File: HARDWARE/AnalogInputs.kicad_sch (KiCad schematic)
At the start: 12 parts, among them U7 MCP6001-OT, U8 MCP6001-OT

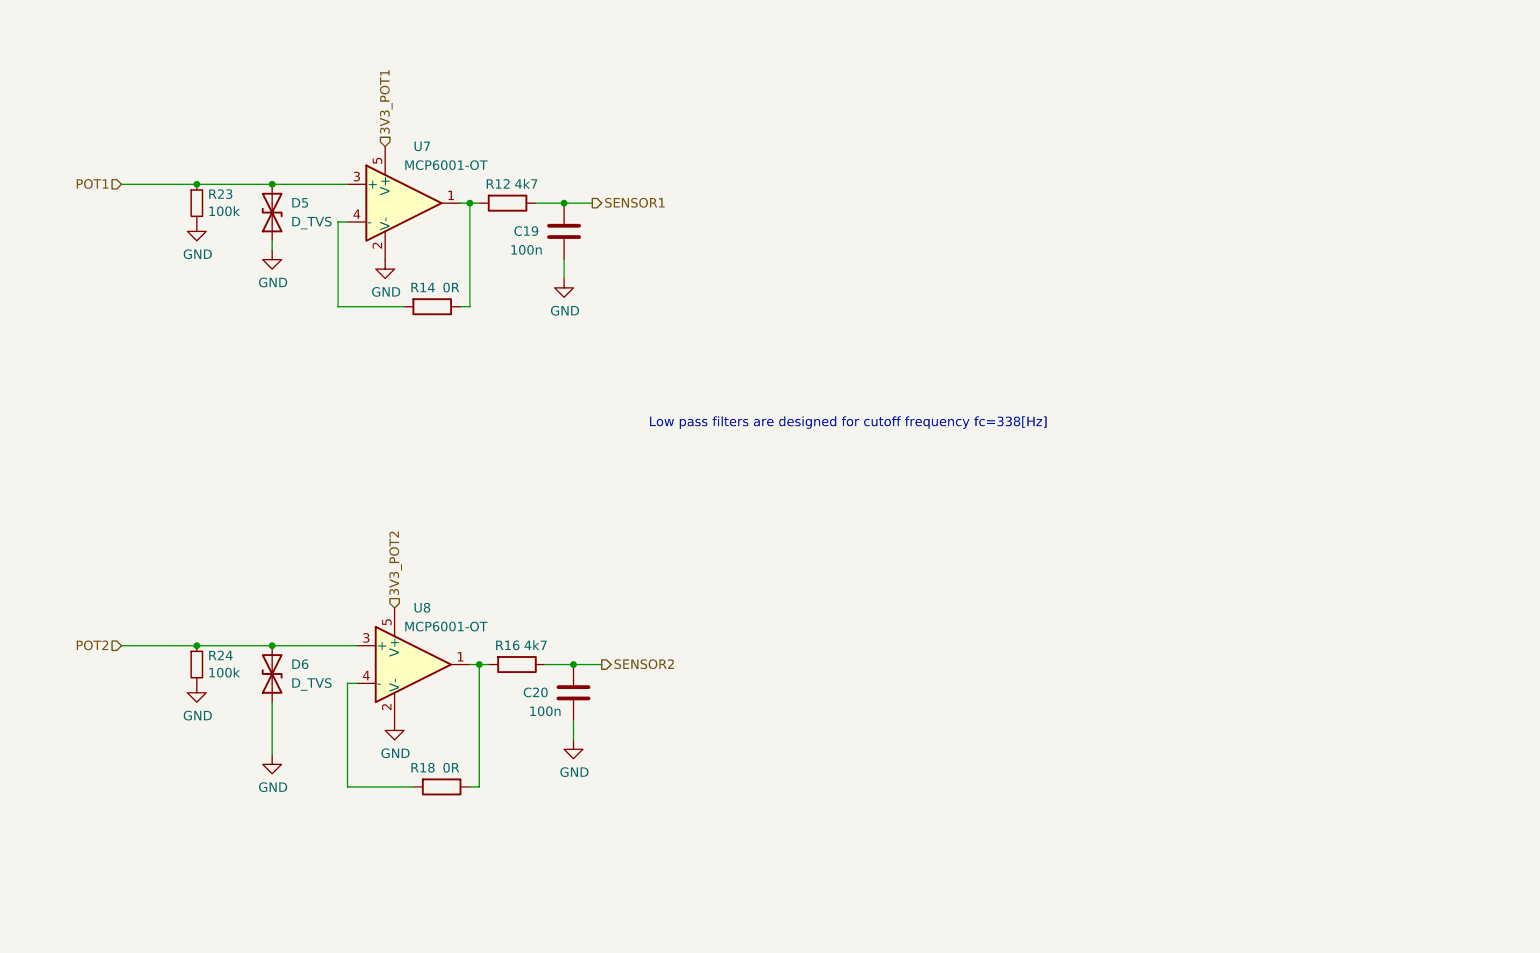
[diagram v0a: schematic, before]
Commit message: Use in-amps for the analog inputs
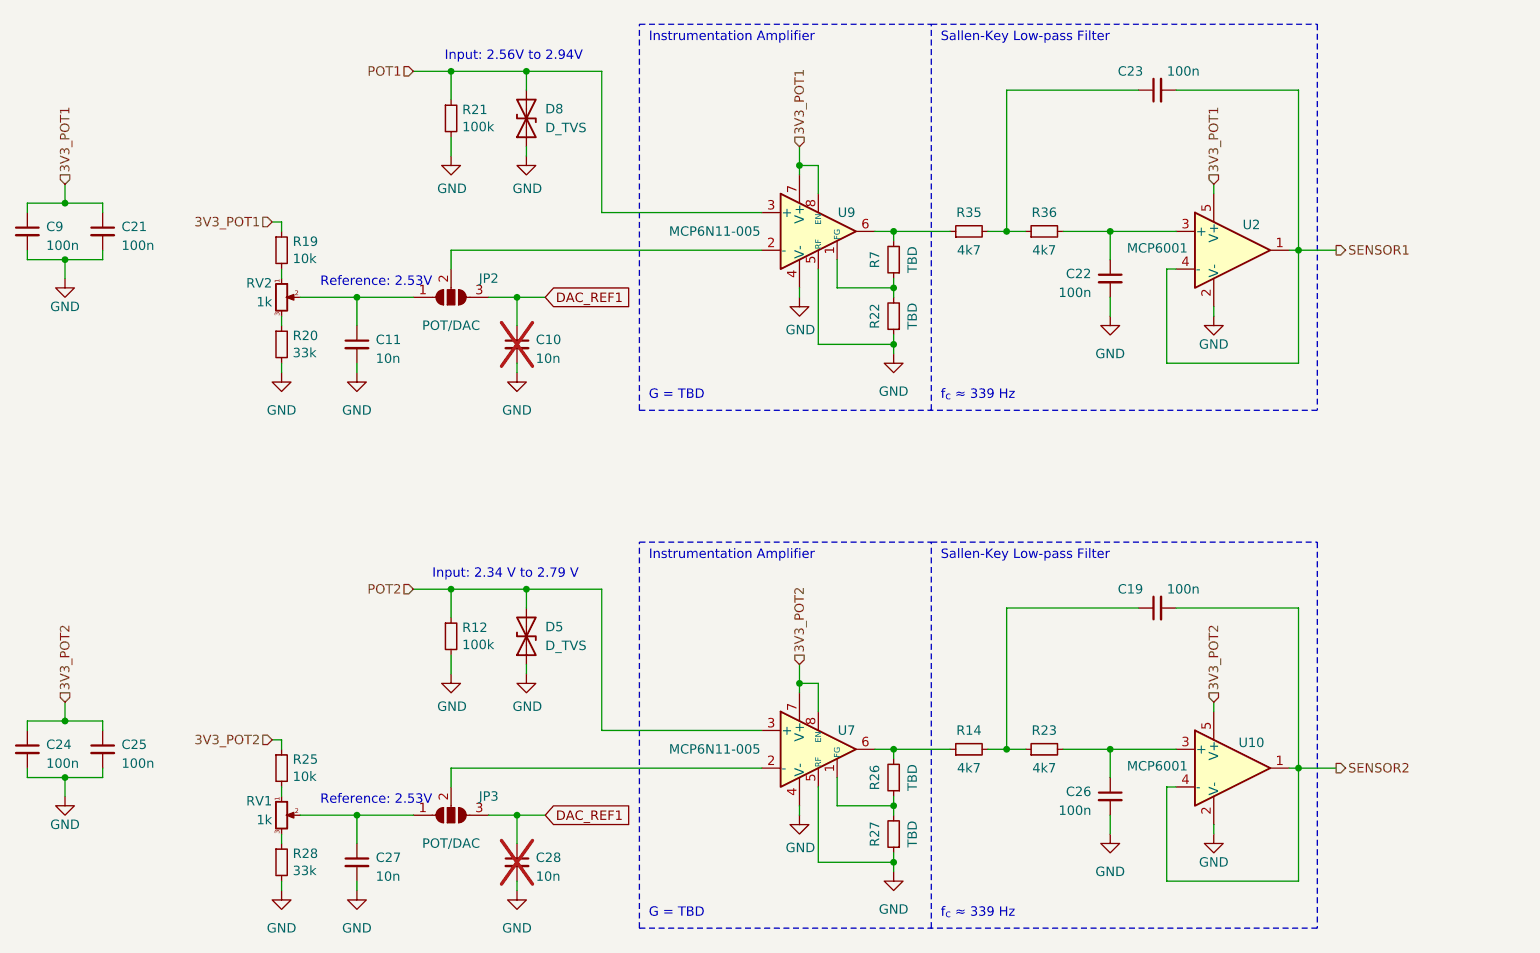
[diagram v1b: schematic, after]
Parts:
- removed C19, C20: 100n, Capacitor_SMD:C_0603_1608Metric_Pad1.08x0.95mm_HandSolder, symbol Device:C
- removed D6: D_TVS, Diode_SMD:D_0603_1608Metric_Pad1.05x0.95mm_HandSolder, symbol Device:D_TVS
- removed R12, R16: 4k7, Resistor_SMD:R_0603_1608Metric_Pad0.98x0.95mm_HandSolder, symbol Device:R
- removed R14, R18: 0R, Resistor_SMD:R_0603_1608Metric_Pad0.98x0.95mm_HandSolder, symbol Device:R
- removed R24: 100k, Resistor_SMD:R_0603_1608Metric_Pad0.98x0.95mm_HandSolder, symbol Device:R_Small
- removed U7, U8: MCP6001-OT, Package_TO_SOT_SMD:SOT-23-5, symbol Amplifier_Operational:MCP6001-OT
- added C10, C11, C27, C28: 10n, symbol Device:C_Small
- added C19, C21, C22, C23, C24, C25, C26, C9: 100n, symbol Device:C_Small
- added D8: D_TVS, Diode_SMD:D_0603_1608Metric_Pad1.05x0.95mm_HandSolder, symbol Device:D_TVS
- added JP2, JP3: POT/DAC, symbol Jumper:SolderJumper_3_Open
- added R12, R21: 100k, Resistor_SMD:R_0603_1608Metric_Pad0.98x0.95mm_HandSolder, symbol Device:R_Small
- added R14, R35, R36: 4k7, symbol Device:R_Small
- added R19, R25: 10k, Resistor_SMD:R_0603_1608Metric_Pad0.98x0.95mm_HandSolder, symbol Device:R_Small
- added R20, R28: 33k, Resistor_SMD:R_0603_1608Metric_Pad0.98x0.95mm_HandSolder, symbol Device:R_Small
- added R22, R26, R27, R7: TBD, symbol Device:R_Small
- added RV1, RV2: 1k, symbol Device:R_Potentiometer_Small
- added U10, U2: MCP6001, Package_TO_SOT_SMD:SOT-23-5, symbol Amplifier_Operational:MCP6001-OT
- added U7, U9: MCP6N11-005, Package_SO:SOIC-8_3.9x4.9mm_P1.27mm, symbol MCP6N11:MCP6N11
- R23: value 100k -> 4k7; footprint Resistor_SMD:R_0603_1608Metric_Pad0.98x0.95mm_HandSolder -> (none)
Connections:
- net 3V3_POT1: now also C21.1, C9.1, R19.1, U2.5 (V+), U9.7 (V+), U9.8 (EN)
- net 3V3_POT2: now also C24.1, C25.1, R25.1, U10.5 (V+), U7.7 (V+), U7.8 (EN)
- net GND: now also C10.2, C11.2, C21.2, C22.2, C24.2, C25.2, C26.2, C27.2, C28.2, C9.2, D8.1 (A1), R12.2, R20.2, R21.2, R22.1, R27.1, R28.2, U10.2 (V-), U2.2 (V-), U7.4 (V-), U7.5 (RF), U9.4 (V-), U9.5 (RF); no longer R23.2
- net POT1: now also D8.2 (A2), R21.1, U9.3 (+); no longer D5.2 (A2), R23.1
- net POT2: now also D5.2 (A2), R12.1, U7.3 (+)
- net SENSOR1: now also C23.2, U2.1, U2.4 (-)
- net SENSOR2: now also C19.2, U10.1, U10.4 (-)
- new net: R19.2, RV2.1
- new net: C11.1, JP2.1 (A), RV2.2
- new net: R20.1, RV2.3
- new net: C22.1, R36.2, U2.3 (+)
- new net: R14.1, R26.2, U7.6
- new net: C19.1, R14.2, R23.1
- new net: R35.1, R7.2, U9.6
- new net: C23.1, R35.2, R36.1
- new net: C26.1, R23.2, U10.3 (+)
- new net: R26.1, R27.2, U7.1 (FG)
- new net: R25.2, RV1.1
- new net: C27.1, JP3.1 (A), RV1.2
- new net: R28.1, RV1.3
- new net: JP3.2 (C), U7.2 (-)
- new net: JP2.2 (C), U9.2 (-)
- new net: R22.2, R7.1, U9.1 (FG)
- new net DAC_REF1: C10.1, C28.1, JP2.3 (B), JP3.3 (B)
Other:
- note added: "G = TBD"
- note added: "Input: 2.34 V to 2.79 V"
- note added: "Input: 2.56V to 2.94V"
- note added: "Instrumentation Amplifier"
- note added: "Reference: 2.53V"
- note added: "Sallen-Key Low-pass Filter"
- note added: "f_{c} ≈ 339 Hz"
- note removed: "Low pass filters are designed for cutoff frequency fc=338[Hz]"

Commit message: Align components on the PCB
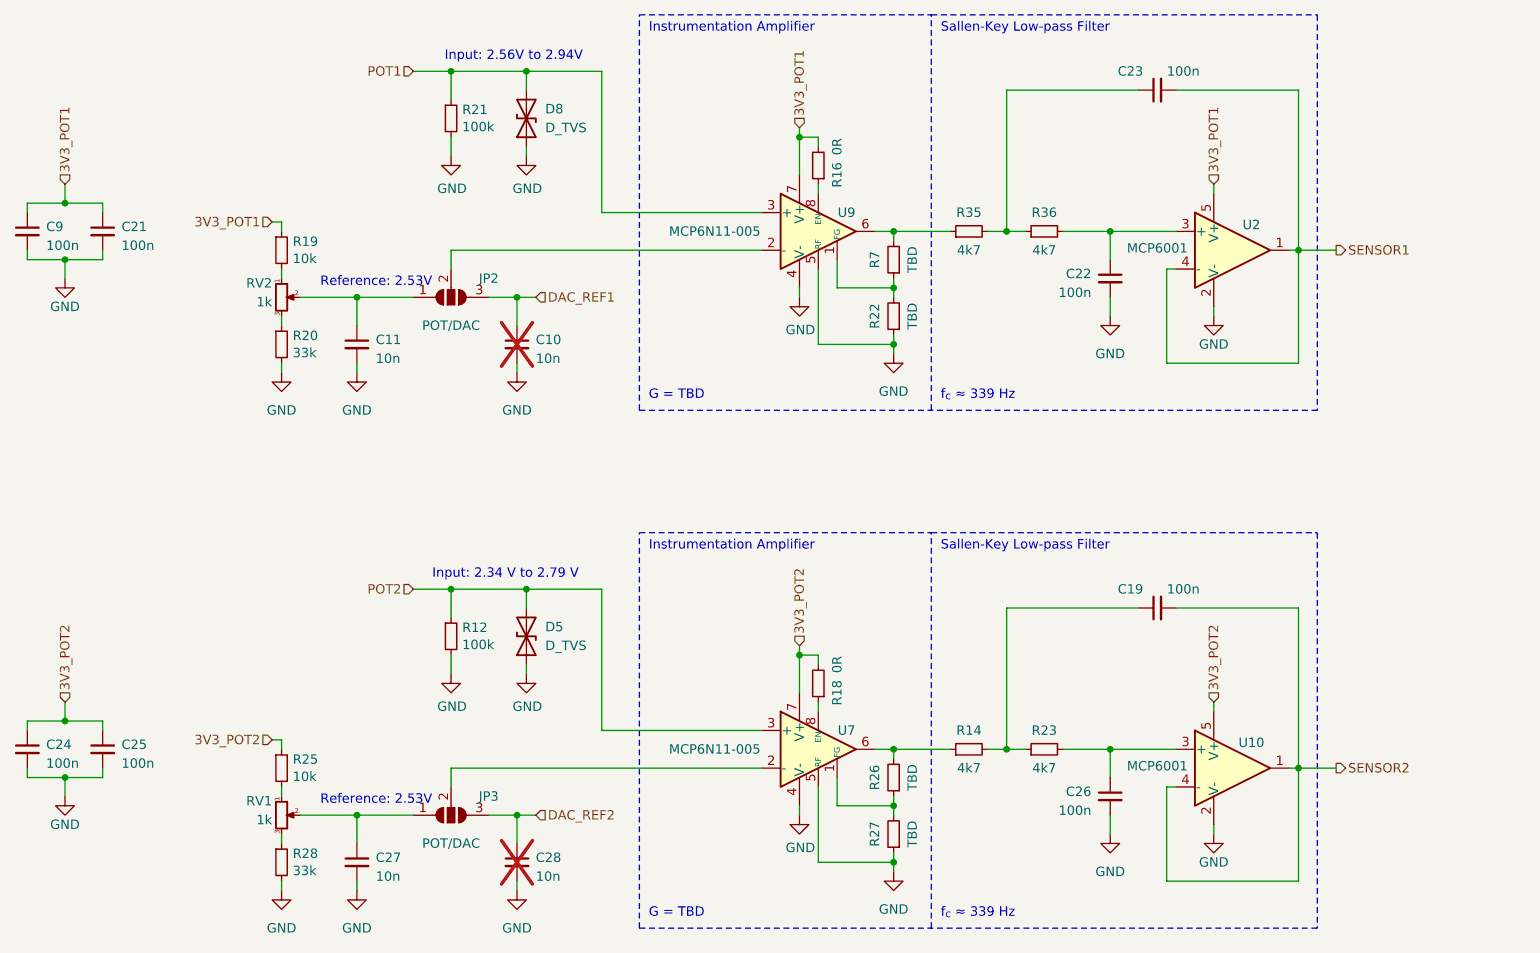
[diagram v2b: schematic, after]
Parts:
- added R16, R18: 0R, Resistor_SMD:R_0603_1608Metric_Pad0.98x0.95mm_HandSolder, symbol Device:R_Small
- C10, C11, C19, C21, C22, C23, C24, C25, C26, C27, C28, C9: footprint (none) -> Capacitor_SMD:C_0603_1608Metric_Pad1.08x0.95mm_HandSolder
- JP2, JP3: footprint (none) -> Jumper:SolderJumper-3_P1.3mm_Open_RoundedPad1.0x1.5mm_NumberLabels
- R14, R22, R23, R26, R27, R35, R36, R7: footprint (none) -> Resistor_SMD:R_0603_1608Metric_Pad0.98x0.95mm_HandSolder
- RV1, RV2: footprint (none) -> Potentiometer_SMD:Potentiometer_Bourns_3214J_Horizontal
- U7, U9: footprint Package_SO:SOIC-8_3.9x4.9mm_P1.27mm -> Package_DFN_QFN:TDFN-8-1EP_3x2mm_P0.5mm_EP1.3x1.4mm
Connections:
- net 3V3_POT1: now also R16.2; no longer U9.8 (EN)
- net 3V3_POT2: now also R18.2; no longer U7.8 (EN)
- net DAC_REF1: no longer C28.1, JP3.3 (B)
- net GND: now also U7.9 (EP), U9.9 (EP)
- new net: R18.1, U7.8 (EN)
- new net: R16.1, U9.8 (EN)
- new net DAC_REF2: C28.1, JP3.3 (B)
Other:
- company: (none) -> PUT Motorsport

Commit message: Route PCB tracks
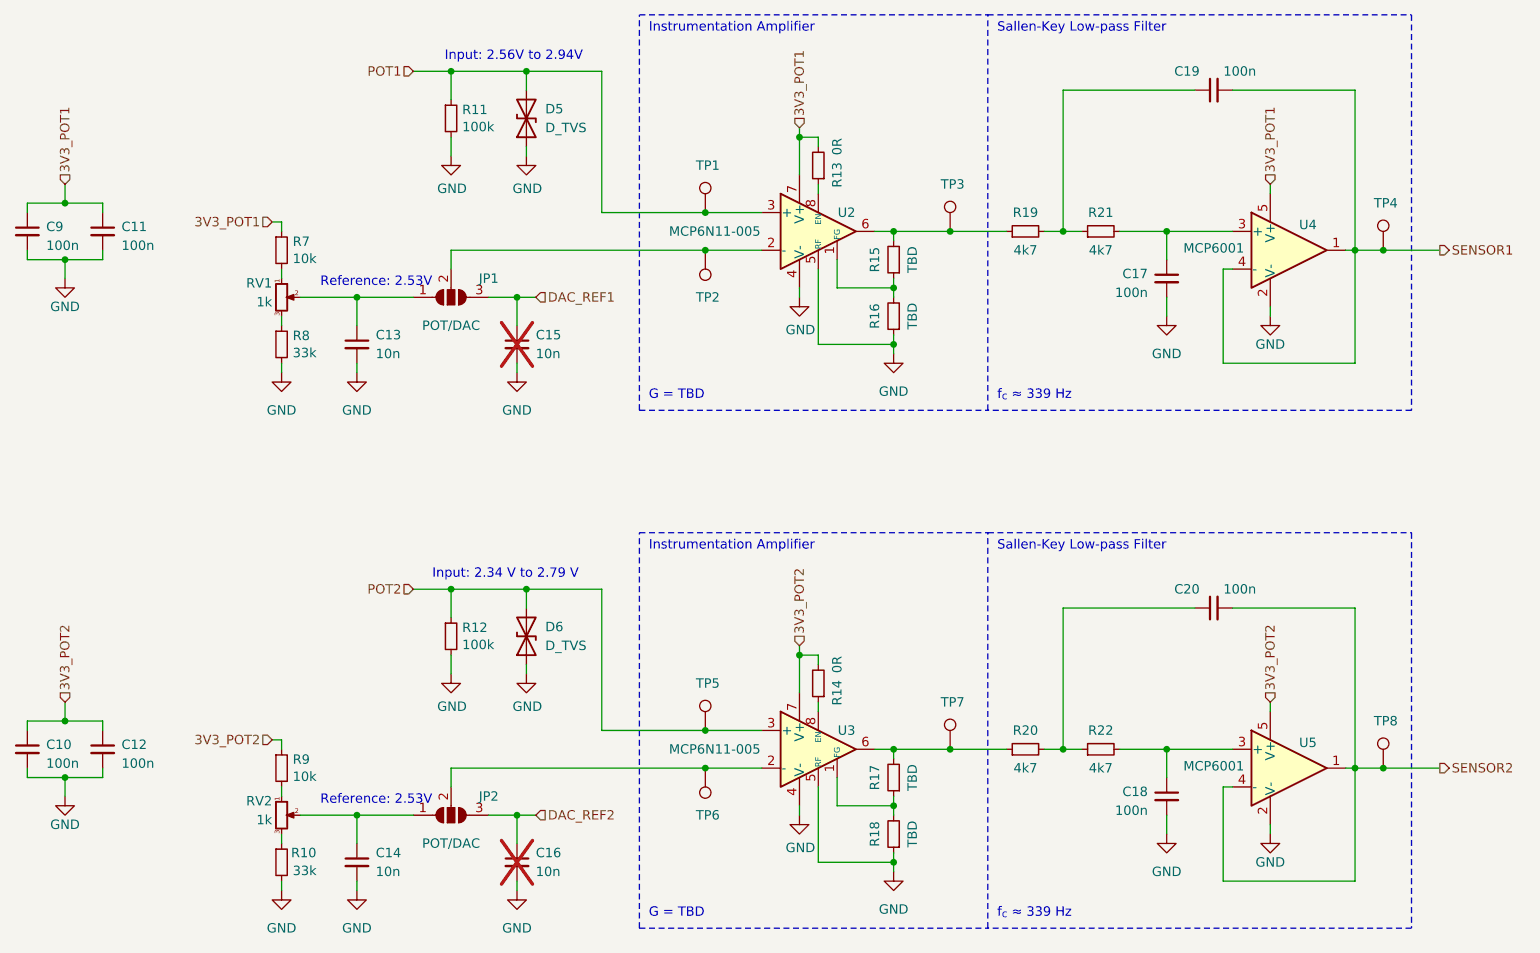
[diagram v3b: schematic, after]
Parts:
- added TP1: P1, TestPoint:TestPoint_Pad_1.0x1.0mm, symbol Connector:TestPoint
- added TP2: N1, TestPoint:TestPoint_Pad_1.0x1.0mm, symbol Connector:TestPoint
- added TP3: O1, TestPoint:TestPoint_Pad_1.0x1.0mm, symbol Connector:TestPoint
- added TP4: F1, TestPoint:TestPoint_Pad_1.0x1.0mm, symbol Connector:TestPoint
- added TP5: P2, TestPoint:TestPoint_Pad_1.0x1.0mm, symbol Connector:TestPoint
- added TP6: N2, TestPoint:TestPoint_Pad_1.0x1.0mm, symbol Connector:TestPoint
- added TP7: O2, TestPoint:TestPoint_Pad_1.0x1.0mm, symbol Connector:TestPoint
- added TP8: F2, TestPoint:TestPoint_Pad_1.0x1.0mm, symbol Connector:TestPoint
- renumbered C24 to C10, C21 to C11, C25 to C12, C11 to C13, C27 to C14, C10 to C15, C28 to C16, C22 to C17, C26 to C18, C23 to C19, C19 to C20, D8 to D5, D5 to D6, JP2 to JP1, JP3 to JP2, R28 to R10, R21 to R11, R16 to R13, R18 to R14, R7 to R15, R22 to R16, R26 to R17, R27 to R18, R35 to R19, R14 to R20, R36 to R21, R23 to R22, R19 to R7, R20 to R8, R25 to R9, RV2 to RV1, RV1 to RV2, U9 to U2, U7 to U3, U2 to U4, U10 to U5
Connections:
- net POT1: now also TP1.1
- net POT2: now also TP5.1
- net SENSOR1: now also TP4.1
- net SENSOR2: now also TP8.1
- net at R17.2, R20.1, U3.6: now also TP7.1
- net at R15.2, R19.1, U2.6: now also TP3.1
- net at JP2.2 (C), U3.2 (-): now also TP6.1
- net at JP1.2 (C), U2.2 (-): now also TP2.1
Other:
- company: PUT Motorsport -> S. Sambor
- moved on the sheet: C17, C18, C19, C20, R19, R20, R21, R22, U4, U5
